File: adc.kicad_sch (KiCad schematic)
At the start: 5 parts, among them U10 TPS7B91033DBVR, U8 MCP3202

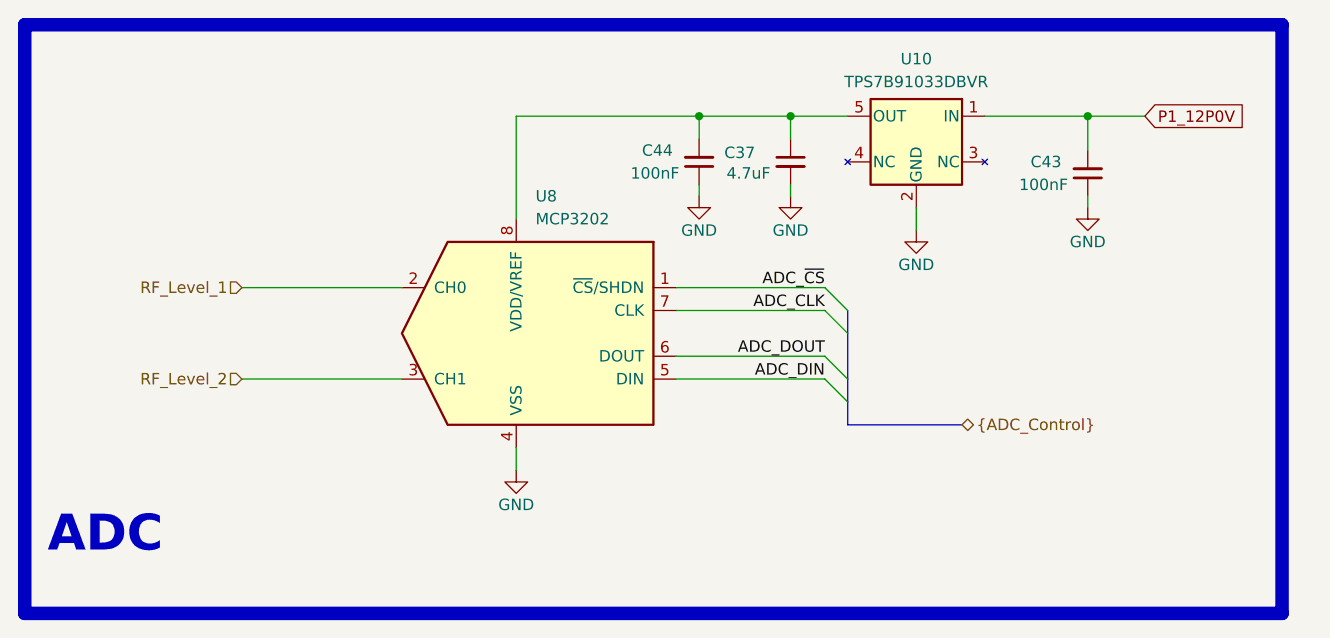
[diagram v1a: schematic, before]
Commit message: Draft Schematic Revision
Schematic should be in good shape.
Meta-data and BOM need to be finished.
Very rough layout was started to floorplan out main parts and to see if we have room.
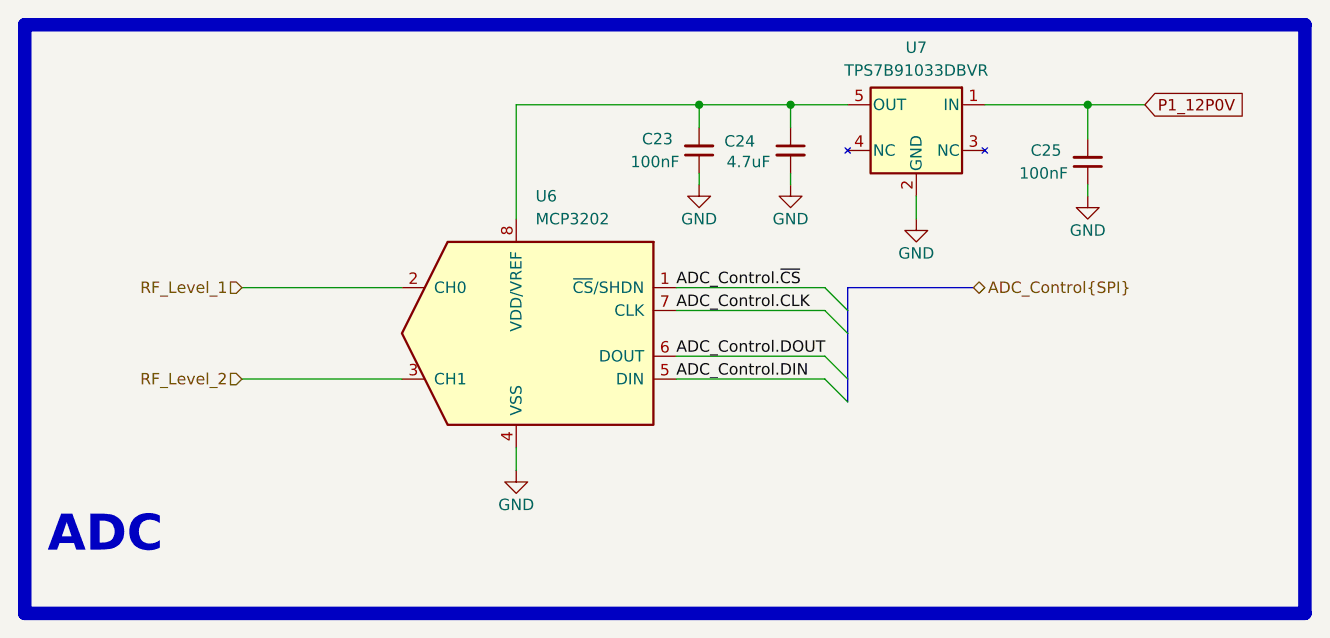
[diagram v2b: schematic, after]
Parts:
- renumbered C44 to C23, C37 to C24, C43 to C25, U8 to U6, U10 to U7
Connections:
- net ADC_CLK renamed ADC_Control.CLK
- net ADC_DIN renamed ADC_Control.DIN
- net ADC_DOUT renamed ADC_Control.DOUT
- net ADC_~{CS} renamed ADC_Control.~{CS}
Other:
- moved on the sheet: C23, C24, C25, U7

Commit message: add copyright/license
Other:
- company: Osprey DCS -> SPDX-FileCopyrightText: 2025 Osprey DCS
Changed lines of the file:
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@@
 		(date "2025-10-01")
 		(rev "0.1")
-		(company "Osprey DCS")
-		(comment 1 "Pedro Rodriguez")
+		(company "SPDX-FileCopyrightText: 2025 Osprey DCS")
+		(comment 1 "SPDX-License-Identifier: CERN-OHL-S-2.0+")
 	)
 	(bus_alias "SPI"

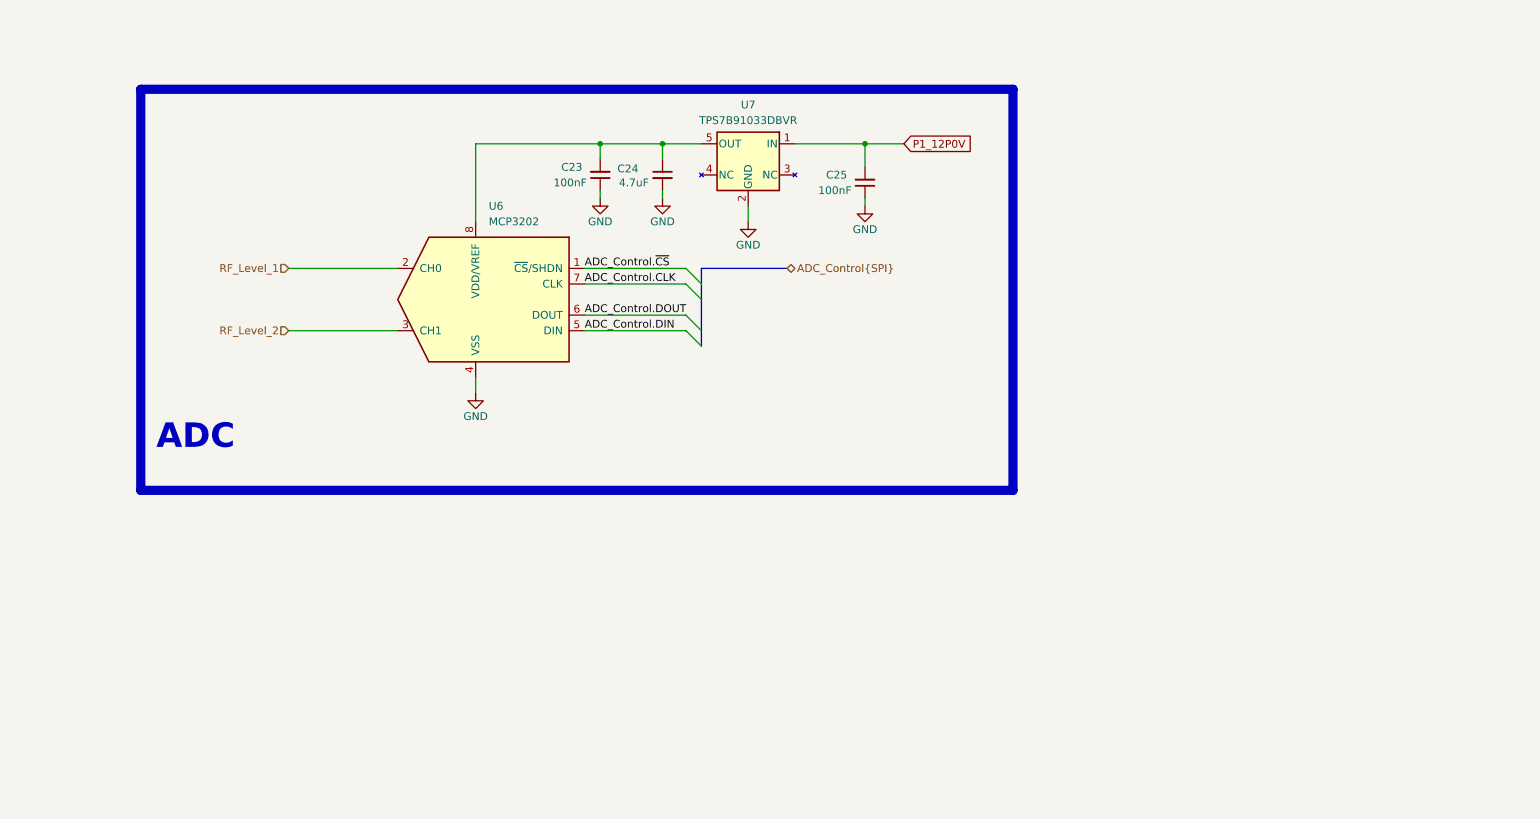
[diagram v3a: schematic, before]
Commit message: Changed ADC and removed Level Shifter
- Changed ADC to ADS7253
- Removed Level Shifters
- Change paper size to US standard sizes for printing
- removed 3d models
- Changed SMA clock input to a 2 pin ISORATE connector
- Floor planned out the PCB layout with the new parts
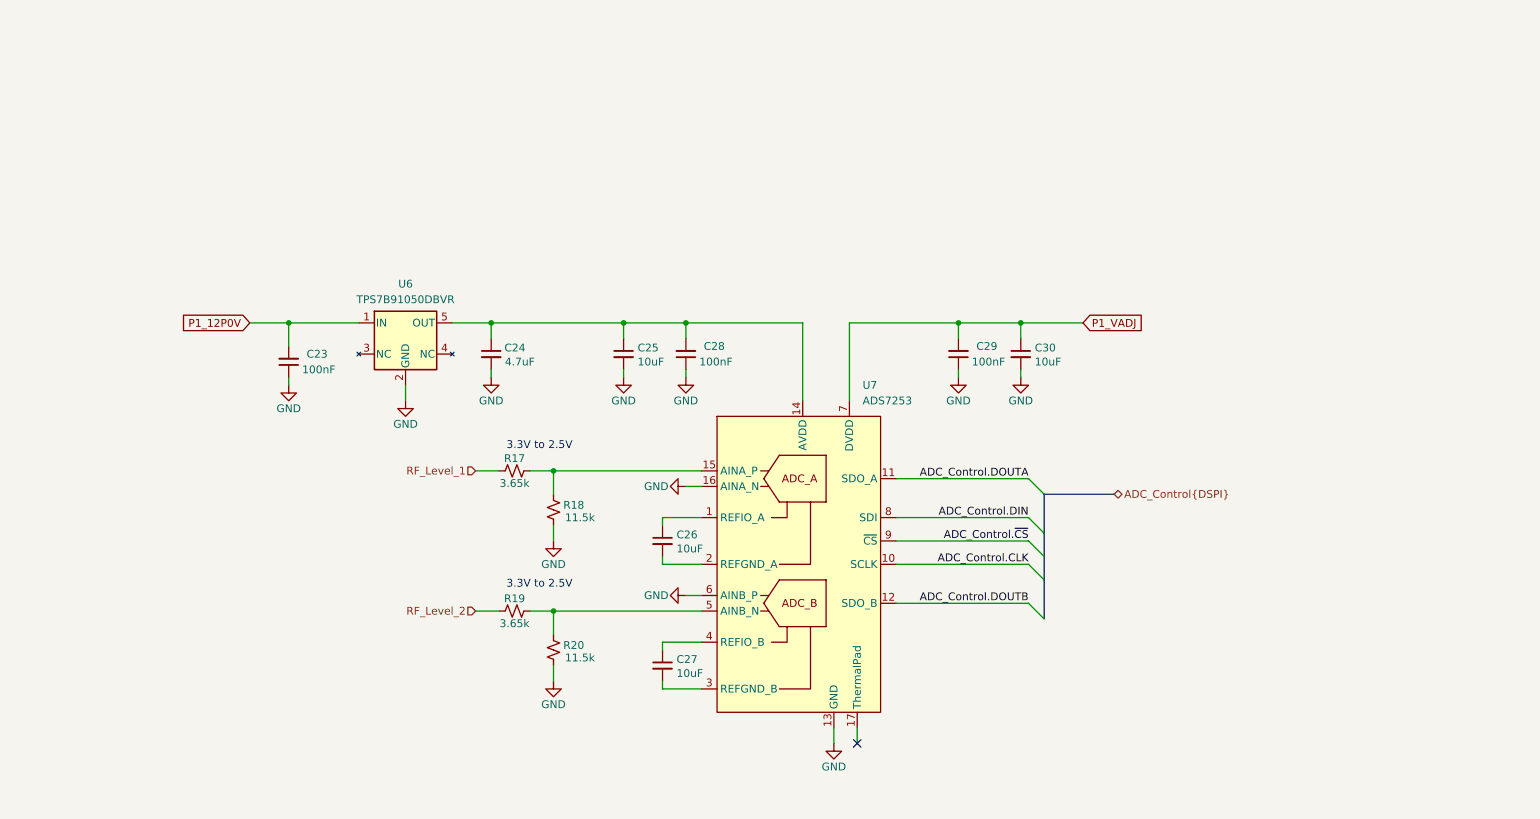
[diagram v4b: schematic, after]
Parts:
- removed U6: MCP3202, Package_SO:TSSOP-8_3x3mm_P0.65mm, symbol Analog_ADC:MCP3202
- added C25, C26, C27, C30: 10uF, Capacitor_SMD:C_0603_1608Metric, symbol Device:C_Small
- added C29: 100nF, Capacitor_SMD:C_0402_1005Metric, symbol Device:C_Small
- added R17, R19: 3.65k, Resistor_SMD:R_0402_1005Metric, symbol Device:R_Small_US
- added R18, R20: 11.5k, Resistor_SMD:R_0402_1005Metric, symbol Device:R_Small_US
- added U7: ADS7253, Package_DFN_QFN:Texas_RTE0016D_WQFN-16-1EP_3x3mm_P0.5mm_EP0.8x0.8mm_ThermalVias, symbol rf-input-fmc:ADS7253
- U6: renamed from U7; value TPS7B91033DBVR -> TPS7B91050DBVR
- renumbered C25 to C23, C23 to C28
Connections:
- net ADC_Control.CLK: now also U7.10 (SCLK)
- net ADC_Control.DIN: now also U7.8 (SDI)
- net ADC_Control.~{CS}: now also U7.9 (~{CS})
- net GND: now also C25.2, C29.1, C30.2, R18.1, R20.1, U7.13 (GND), U7.16 (AINA_N), U7.6 (AINB_P)
- net RF_Level_1: now also R17.1
- net RF_Level_2: now also R19.1
- net at C24.1, C28.2, U6.5 (OUT): now also C25.1, U7.14 (AVDD)
- new net: C26.1, U7.1 (REFIO_A)
- new net: C26.2, U7.2 (REFGND_A)
- new net: C27.1, U7.4 (REFIO_B)
- new net: C27.2, U7.3 (REFGND_B)
- new net: R17.2, R18.2, U7.15 (AINA_P)
- new net: R19.2, R20.2, U7.5 (AINB_N)
- new net ADC_Control.DOUTA: U7.11 (SDO_A)
- new net ADC_Control.DOUTB: U7.12 (SDO_B)
- new net P1_VADJ: C29.2, C30.1, U7.7 (DVDD)
- no-connect marks 0 -> 1
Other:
- note added: "3.3V to 2.5V"
- note removed: "ADC"
- moved on the sheet: C23, C24, C28, U6

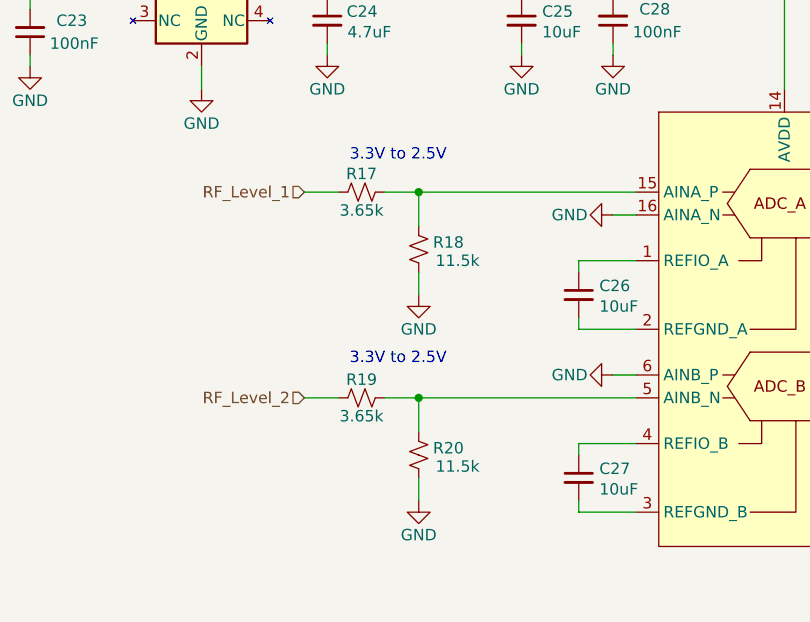
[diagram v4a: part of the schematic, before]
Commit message: Final Schmatic Draft
-Changed ADC
-Changed Digital IO Translator
-Updated all MPNs
- Reannoted Schematic
- Updated Design Document
- Added new Datasheet Document
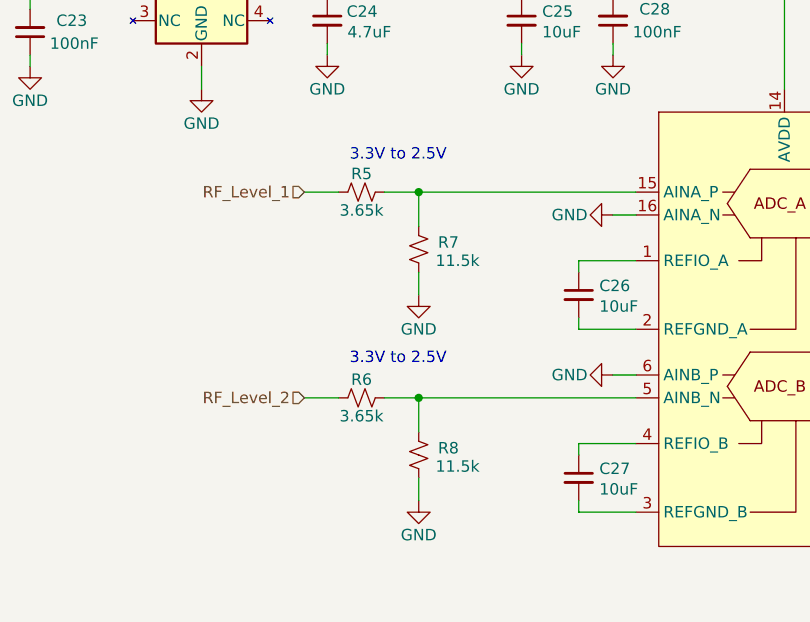
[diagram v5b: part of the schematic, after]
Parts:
- U6: MPN (none) -> TPS7B92050DBVR; Manufacturer (none) -> Texas Instruments
- U7: MPN (none) -> ADS7253IRTET; Manufacturer (none) -> Texas Instruments
- renumbered R17 to R5, R19 to R6, R18 to R7, R20 to R8
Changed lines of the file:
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@@
 		(on_board yes)
 		(dnp no)
-		(property "Reference" "#PWR058"
+		(property "Reference" "#PWR018"
 			(at 102.87 109.22 0)
 			(effects
@@
 			(project "rf-input-fmc"
 				(path "/1719e569-47c8-4fa0-8523-9c9686ef0dba/d098b615-7cba-44eb-be59-7a71f2f48c2b"
-					(reference "#PWR058")
+					(reference "#PWR018")
 					(unit 1)
 				)
@@
 		(on_board yes)
 		(dnp no)
-		(property "Reference" "#PWR020"
+		(property "Reference" "#PWR022"
 			(at 118.11 93.98 0)
 			(effects
@@
 			(project "rf-input-fmc"
 				(path "/1719e569-47c8-4fa0-8523-9c9686ef0dba/d098b615-7cba-44eb-be59-7a71f2f48c2b"
-					(reference "#PWR020")
+					(reference "#PWR022")
 					(unit 1)
 				)
@@
 			)
 		)
-		(property "Datasheet" ""
+		(property "Datasheet" "~"
 			(at 120.65 102.87 0)
 			(effects
@@
 			)
 		)
-		(property "Datasheet" ""
+		(property "Datasheet" "~"
 			(at 114.3 72.39 0)
 			(effects
@@
 		(on_board yes)
 		(dnp no)
-		(property "Reference" "#PWR059"
+		(property "Reference" "#PWR019"
 			(at 102.87 132.08 0)
 			(effects
@@
 			(project "rf-input-fmc"
 				(path "/1719e569-47c8-4fa0-8523-9c9686ef0dba/d098b615-7cba-44eb-be59-7a71f2f48c2b"
-					(reference "#PWR059")
+					(reference "#PWR019")
 					(unit 1)
 				)
@@
 			)
 		)
-		(property "Datasheet" ""
+		(property "Datasheet" "~"
 			(at 179.07 72.39 0)
 			(effects
@@
 			)
 		)
-		(property "Datasheet" ""
+		(property "Datasheet" "~"
 			(at 120.65 123.19 0)
 			(effects
@@
 		(on_board yes)
 		(dnp no)
-		(property "Reference" "R18"
+		(property "Reference" "R7"
 			(at 106.172 97.028 0)
 			(effects
@@
 			(project "rf-input-fmc"
 				(path "/1719e569-47c8-4fa0-8523-9c9686ef0dba/d098b615-7cba-44eb-be59-7a71f2f48c2b"
-					(reference "R18")
+					(reference "R7")
 					(unit 1)
 				)
@@
 			)
 		)
+		(property "MPN" "TPS7B92050DBVR"
+			(at 78.74 69.85 0)
+			(effects
+				(font
+					(size 1.27 1.27)
+				)
+				(hide yes)
+			)
+		)
+		(property "Manufacturer" "Texas Instruments"
+			(at 78.74 69.85 0)
+			(effects
+				(font
+					(size 1.27 1.27)
+				)
+				(hide yes)
+			)
+		)
 		(pin "1"
 		)
@@
 		(on_board yes)
 		(dnp no)
-		(property "Reference" "#PWR018"
+		(property "Reference" "#PWR020"
 			(at 114.3 82.55 0)
 			(effects
@@
 			(project "rf-input-fmc"
 				(path "/1719e569-47c8-4fa0-8523-9c9686ef0dba/d098b615-7cba-44eb-be59-7a71f2f48c2b"
-					(reference "#PWR018")
+					(reference "#PWR020")
 					(unit 1)
 				)
@@
 		(on_board yes)
 		(dnp no)
-		(property "Reference" "#PWR022"
+		(property "Reference" "#PWR024"
 			(at 148.59 142.24 0)
 			(effects
@@
 			(project "rf-input-fmc"
 				(path "/1719e569-47c8-4fa0-8523-9c9686ef0dba/d098b615-7cba-44eb-be59-7a71f2f48c2b"
-					(reference "#PWR022")
+					(reference "#PWR024")
 					(unit 1)
 				)
@@
 		(on_board yes)
 		(dnp no)
-		(property "Reference" "R19"
+		(property "Reference" "R6"
 			(at 96.52 112.268 90)
 			(effects
@@
 			(project "rf-input-fmc"
 				(path "/1719e569-47c8-4fa0-8523-9c9686ef0dba/d098b615-7cba-44eb-be59-7a71f2f48c2b"
-					(reference "R19")
+					(reference "R6")
 					(unit 1)
 				)
@@
 		(on_board yes)
 		(dnp no)
-		(property "Reference" "#PWR019"
+		(property "Reference" "#PWR021"
 			(at 124.46 82.55 0)
 			(effects
@@
 			(project "rf-input-fmc"
 				(path "/1719e569-47c8-4fa0-8523-9c9686ef0dba/d098b615-7cba-44eb-be59-7a71f2f48c2b"
-					(reference "#PWR019")
+					(reference "#PWR021")
 					(unit 1)
 				)
@@
 		(on_board yes)
 		(dnp no)
-		(property "Reference" "R17"
+		(property "Reference" "R5"
 			(at 96.52 89.408 90)
 			(effects
@@
 			(project "rf-input-fmc"
 				(path "/1719e569-47c8-4fa0-8523-9c9686ef0dba/d098b615-7cba-44eb-be59-7a71f2f48c2b"
-					(reference "R17")
+					(reference "R5")
 					(unit 1)
 				)
@@
 		(on_board yes)
 		(dnp no)
-		(property "Reference" "#PWR021"
+		(property "Reference" "#PWR023"
 			(at 118.11 111.76 0)
 			(effects
@@
 			(project "rf-input-fmc"
 				(path "/1719e569-47c8-4fa0-8523-9c9686ef0dba/d098b615-7cba-44eb-be59-7a71f2f48c2b"
-					(reference "#PWR021")
+					(reference "#PWR023")
 					(unit 1)
 				)
@@
 		(on_board yes)
 		(dnp no)
-		(property "Reference" "#PWR023"
+		(property "Reference" "#PWR025"
 			(at 168.91 82.55 0)
 			(effects
@@
 			(project "rf-input-fmc"
 				(path "/1719e569-47c8-4fa0-8523-9c9686ef0dba/d098b615-7cba-44eb-be59-7a71f2f48c2b"
-					(reference "#PWR023")
+					(reference "#PWR025")
 					(unit 1)
 				)
@@
 		(on_board yes)
 		(dnp no)
-		(property "Reference" "#PWR024"
+		(property "Reference" "#PWR026"
 			(at 179.07 82.55 0)
 			(effects
@@
 			(project "rf-input-fmc"
 				(path "/1719e569-47c8-4fa0-8523-9c9686ef0dba/d098b615-7cba-44eb-be59-7a71f2f48c2b"
-					(reference "#PWR024")
+					(reference "#PWR026")
 					(unit 1)
 				)
@@
 			)
 		)
+		(property "MPN" "ADS7253IRTET"
+			(at 129.54 82.55 0)
+			(effects
+				(font
+					(size 1.27 1.27)
+				)
+				(hide yes)
+			)
+		)
+		(property "Manufacturer" "Texas Instruments"
+			(at 129.54 82.55 0)
+			(effects
+				(font
+					(size 1.27 1.27)
+				)
+				(hide yes)
+			)
+		)
 		(pin "4"
 		)
@@
 		(on_board yes)
 		(dnp no)
-		(property "Reference" "R20"
+		(property "Reference" "R8"
 			(at 106.172 119.888 0)
 			(effects
@@
 			(project "rf-input-fmc"
 				(path "/1719e569-47c8-4fa0-8523-9c9686ef0dba/d098b615-7cba-44eb-be59-7a71f2f48c2b"
-					(reference "R20")
-					(unit 1)
-				)
+					(reference "R8")
+					(unit 1)
+				)
